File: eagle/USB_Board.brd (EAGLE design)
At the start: 62 x 29 mm, 29 parts, among them IC3 MEGA8-AI, Q2 20MHz, X1 USBPTH

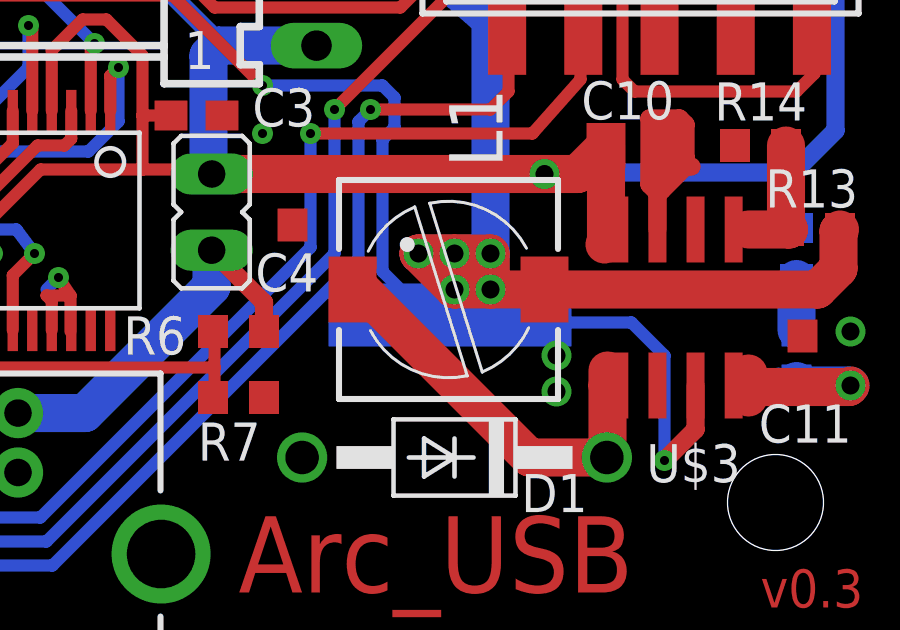
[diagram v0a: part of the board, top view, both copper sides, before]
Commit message: Removed a stupid error from the pcbs and included an instructions file. Switched the firmware to use just two switches instead of four. No one's gonna build an arc16 anyway.
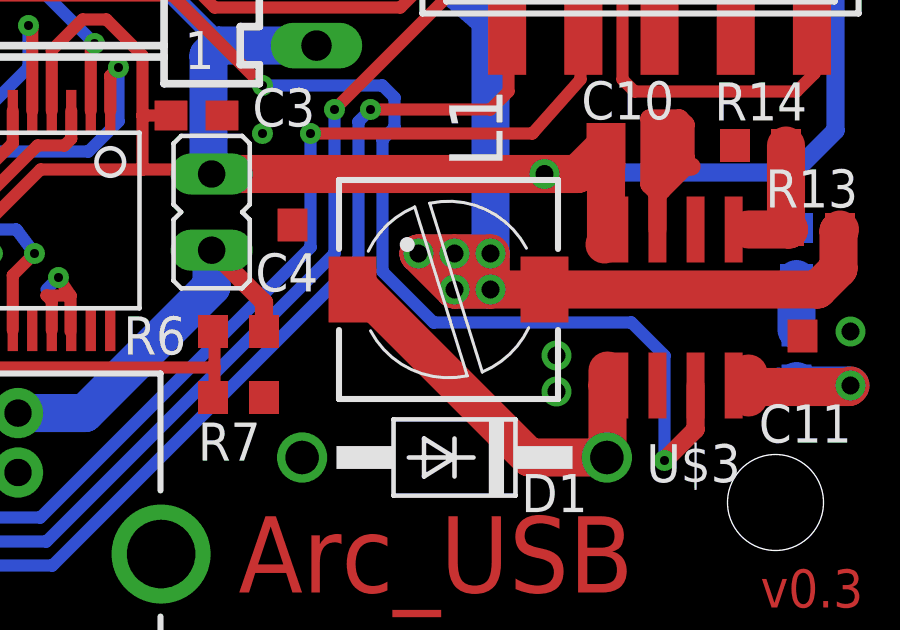
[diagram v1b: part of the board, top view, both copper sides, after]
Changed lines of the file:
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@@
 <layer number="19" name="Unrouted" color="6" fill="1" visible="no" active="yes"/>
 <layer number="20" name="Dimension" color="15" fill="1" visible="yes" active="yes"/>
-<layer number="21" name="tPlace" color="7" fill="1" visible="yes" active="yes"/>
+<layer number="21" name="tPlace" color="7" fill="1" visible="no" active="yes"/>
 <layer number="22" name="bPlace" color="7" fill="1" visible="yes" active="yes"/>
-<layer number="23" name="tOrigins" color="15" fill="1" visible="yes" active="yes"/>
+<layer number="23" name="tOrigins" color="15" fill="1" visible="no" active="yes"/>
 <layer number="24" name="bOrigins" color="15" fill="1" visible="yes" active="yes"/>
 <layer number="25" name="tNames" color="7" fill="1" visible="yes" active="yes"/>
@@
 <wire x1="23.8" y1="24.2" x2="38.2" y2="24.2" width="0.3048" layer="51"/>
 <wire x1="38.2" y1="24.2" x2="38.2" y2="27.8" width="0.3048" layer="51"/>
-<rectangle x1="42.6" y1="9.7" x2="50.7" y2="11.8" layer="16"/>
 </plain>
 <attributes>
